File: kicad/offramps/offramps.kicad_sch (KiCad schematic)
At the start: 224 parts, among them J10 Conn_01x04_Socket, J11 Screw_Terminal_01x02, J12 Conn_01x04_Pin, J13 Micro_SD_Card, J14 Conn_01x03_Male, J15 Screw_Terminal_01x02, J16 Conn_01x02_Pin, J17 Conn_01x02_Pin, J3 VITA_57.1_FMC_HPC_Carrier, J4 Conn_01x02_Pin, J5 Conn_Coaxial, J6 Conn_01x03_Male, J7 Conn_Coaxial, J8 Conn_Coaxial, J9 Conn_01x06_Male, Q1 BSS138, Q10 BSS138, Q11 BSS138, Q12 BSS138, Q13 NPN, Q14 NPN, Q15 NPN, Q16 NPN, Q17 BSS138, Q18 BSS138, Q19 NPN, Q2 BSS138, Q25 BSS138, Q26 BSS138, Q27 BSS138, Q28 BSS138, Q29 BSS138, Q3 BSS138, Q30 BSS138, Q4 BSS138, Q5 BSS138, Q6 BSS138, Q7 BSS138, Q8 BSS138, Q9 BSS138, SW1 219-8MST, U1 TXB0108PWR, U10 MCP4725xxx-xCH, U11 LMH6611MK/NOPB, U12 ADC1173CIMTC/NOPB, U13 MCP4725xxx-xCH, U14 POPA2994IDGKR, U15 ADS1114IDGS, U16 LIS2MDLTR, U17 LSM6DSRTR, U18 LTC-4627JR, U19 AMS1117-3.3, U2 TXB0108PWR, U20 LM358DR2G, U3 TXB0108PWR, U4 TXB0108PWR, U5 TXB0108PWR, U6 LMH6611MK/NOPB, U7 ADC1175CIMTC/NOPB, U8 TXB0108PWR, U9 PTMUX4053PWR

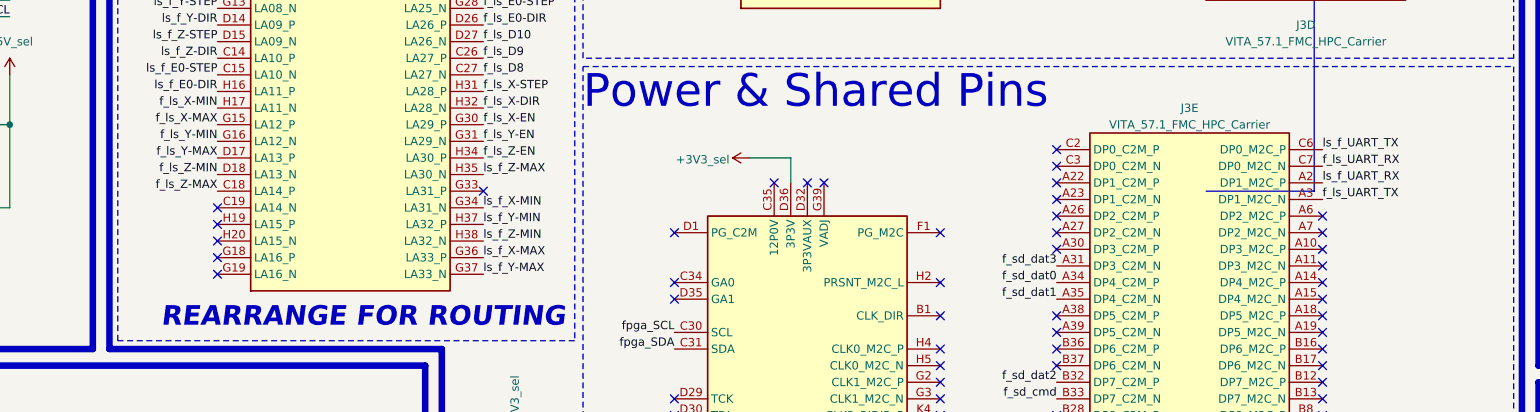
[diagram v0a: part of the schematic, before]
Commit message: Update: Moved UART lines to LPC
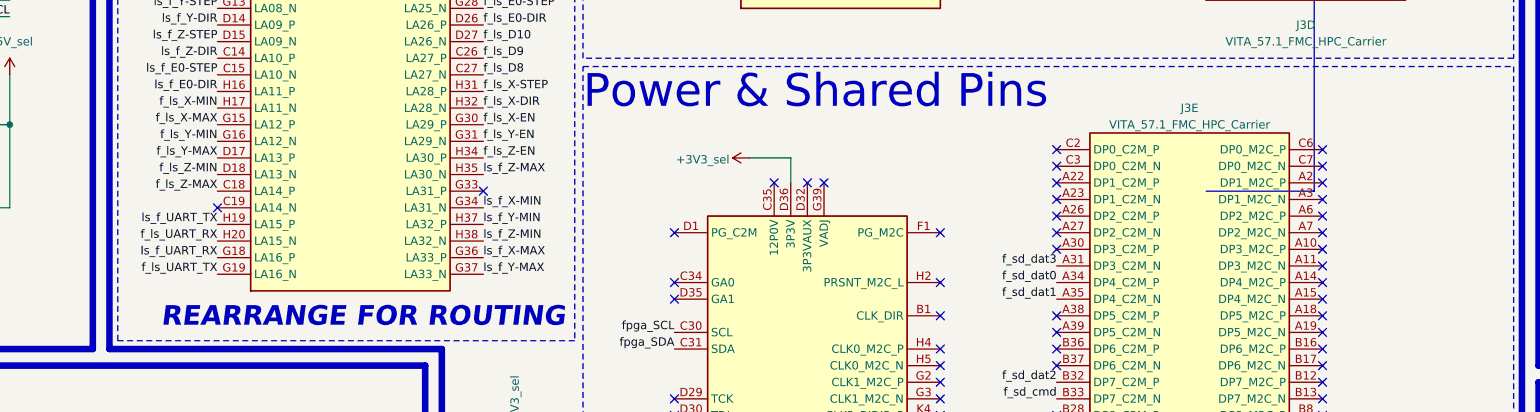
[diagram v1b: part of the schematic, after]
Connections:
- net f_ls_UART_RX: now also J3.H20 (LA15_N); no longer J3.C7 (DP0_M2C_N)
- net f_ls_UART_TX: now also J3.G19 (LA16_N); no longer J3.A3 (DP1_M2C_N)
- net ls_f_UART_RX: now also J3.G18 (LA16_P); no longer J3.A2 (DP1_M2C_P)
- net ls_f_UART_TX: now also J3.H19 (LA15_P); no longer J3.C6 (DP0_M2C_P)
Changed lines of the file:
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@@
 	)
 	(no_connect
+		(at 368.3 132.08)
+	)
+	(no_connect
 		(at 199.39 74.93)
 	)
@@
 	)
 	(no_connect
+		(at 368.3 137.16)
+	)
+	(no_connect
 		(at 368.3 180.34)
 	)
@@
 	)
 	(no_connect
+		(at 368.3 134.62)
+	)
+	(no_connect
+		(at 368.3 139.7)
+	)
+	(no_connect
 		(at 368.3 193.04)
 	)
@@
 	)
 	(no_connect
-		(at 199.39 151.13)
-	)
-	(no_connect
 		(at 368.3 149.86)
 	)
@@
 	)
 	(no_connect
-		(at 199.39 146.05)
-	)
-	(no_connect
 		(at 309.88 144.78)
 	)
 	(no_connect
-		(at 199.39 148.59)
-	)
-	(no_connect
 		(at 269.24 152.4)
 	)
@@
 	)
 	(no_connect
-		(at 199.39 143.51)
-	)
-	(no_connect
 		(at 436.88 148.59)
 	)
@@
 	)
 	(label "ls_f_UART_TX"
-		(at 368.3 132.08 0)
+		(at 199.39 143.51 180)
 		(fields_autoplaced yes)
 		(effects
@@
 				(size 1.27 1.27)
 			)
-			(justify left bottom)
+			(justify right bottom)
 		)
 	)
@@
 	)
 	(label "f_ls_UART_TX"
-		(at 368.3 139.7 0)
+		(at 199.39 151.13 180)
 		(fields_autoplaced yes)
 		(effects
@@
 				(size 1.27 1.27)
 			)
-			(justify left bottom)
+			(justify right bottom)
 		)
 	)
@@
 	)
 	(label "ls_f_UART_RX"
-		(at 368.3 137.16 0)
+		(at 199.39 148.59 180)
 		(fields_autoplaced yes)
 		(effects
@@
 				(size 1.27 1.27)
 			)
-			(justify left bottom)
+			(justify right bottom)
 		)
 	)
@@
 	)
 	(label "f_ls_UART_RX"
-		(at 368.3 134.62 0)
+		(at 199.39 146.05 180)
 		(fields_autoplaced yes)
 		(effects
@@
 				(size 1.27 1.27)
 			)
-			(justify left bottom)
+			(justify right bottom)
 		)
 	)

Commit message: Almost done. Need to flip the FMC connector.
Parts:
- removed J13: Micro_SD_Card, Connector_Card:microSD_HC_Wuerth_693072010801, symbol Connector:Micro_SD_Card
- added J13: Micro_SD_Card_Det1, offramps_lib:SIM-SMD_GT-TF003-H0185-02, symbol Connector:Micro_SD_Card_Det1
- added R80: NP, Resistor_SMD:R_0805_2012Metric, symbol Device:R
- C11, C12, C13, C14, C15, C18, C19, C20, C22, C25, C26, C29, C30, C31: value 100n -> 0.1u; Vendor (none) -> C49678
- C16, C17, C27, C28: Vendor (none) -> C377773
- C32, C34, C36, C38: value 100nF -> 0.1u
- C33: value 10uF -> 10u; Vendor ? -> C440198
- C35: value 220nF -> 220n
- C37: value 100n -> 0.1u
- C39: value 1uF -> 1u
- C43, C44, C45, C46: Vendor (none) -> C440198
- L1, L2: Vendor (none) -> C1046
- Q1, Q10, Q11, Q12, Q17, Q18, Q2, Q25, Q26, Q27, Q28, Q29, Q3, Q30, Q4, Q5, Q6, Q7, Q8, Q9: Vendor (none) -> C2938375
- Q13, Q14, Q15, Q16, Q19: Vendor (none) -> C141788
- R10, R12, R13, R14, R15, R16, R17, R18, R19, R2, R20, R21, R22, R23, R24, R3, R34, R40, R41, R45, R48, R49, R5, R53, R54, R58, R59, R6, R72, R73, R74, R75, R76, R77, R79, R8, R9: Vendor (none) -> C17414
- R11, R26: value 10R -> 10; Vendor (none) -> C17415
- R25, R30: Vendor (none) -> C17594
- R27, R31: Vendor (none) -> C17590
- R32, R33, R52, R57: value 10K -> 10k
- R35, R36, R37, R38, R42, R43, R44, R46, R61: Vendor (none) -> C17408
- R39, R47: Vendor (none) -> C2828783
- R56, R66, R68, R71: Vendor (none) -> C17513
- R64: Vendor (none) -> C17710
- R67, R69, R70, R78: Vendor (none) -> C17477
- SW1: value 219-8MST -> 219-8MSTR; Vendor (none) -> C2842674
- U11, U6: Vendor (none) -> C132099
- U12: value ADC1173CIMTC/NOPB -> ADC1173CIMTCX/NOPB; Vendor (none) -> C701593
- U14: value POPA2994IDGKR -> OPA2994IDGKR; Vendor (none) -> C22399234
- U15: value ADS1114IDGS -> ADS1114IDGSR; Vendor (none) -> C174291
- U7: value ADC1175CIMTC/NOPB -> ADC1175-50CIMTCX/NOPB; Vendor (none) -> C91171
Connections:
- net +3V3_filt: now also C25.1, U11.5 (~DIS), U11.6 (V+); no longer C22.1
- net +3V3_sel: now also C22.1, J13.4 (VDD), R80.1
- net +5V_filt: no longer C25.1, U11.5 (~DIS), U11.6 (V+)
- net GND: now also J13.10 (SHIELD), J13.6 (VSS)
- net f_sd_clk: now also J13.5 (CLK)
- net f_sd_cmd: now also J13.3 (CMD)
- net f_sd_dat0: now also J13.7 (DAT0)
- net f_sd_dat1: now also J13.8 (DAT1)
- net f_sd_dat2: now also J13.1 (DAT2)
- net f_sd_dat3: now also J13.2 (DAT3/CD)
- net f_sd_det: now reaches J3.A38 (DP5_C2M_P)
- net f_sd_det: now also J13.9 (DET), R80.2
- no-connect marks 139 -> 138

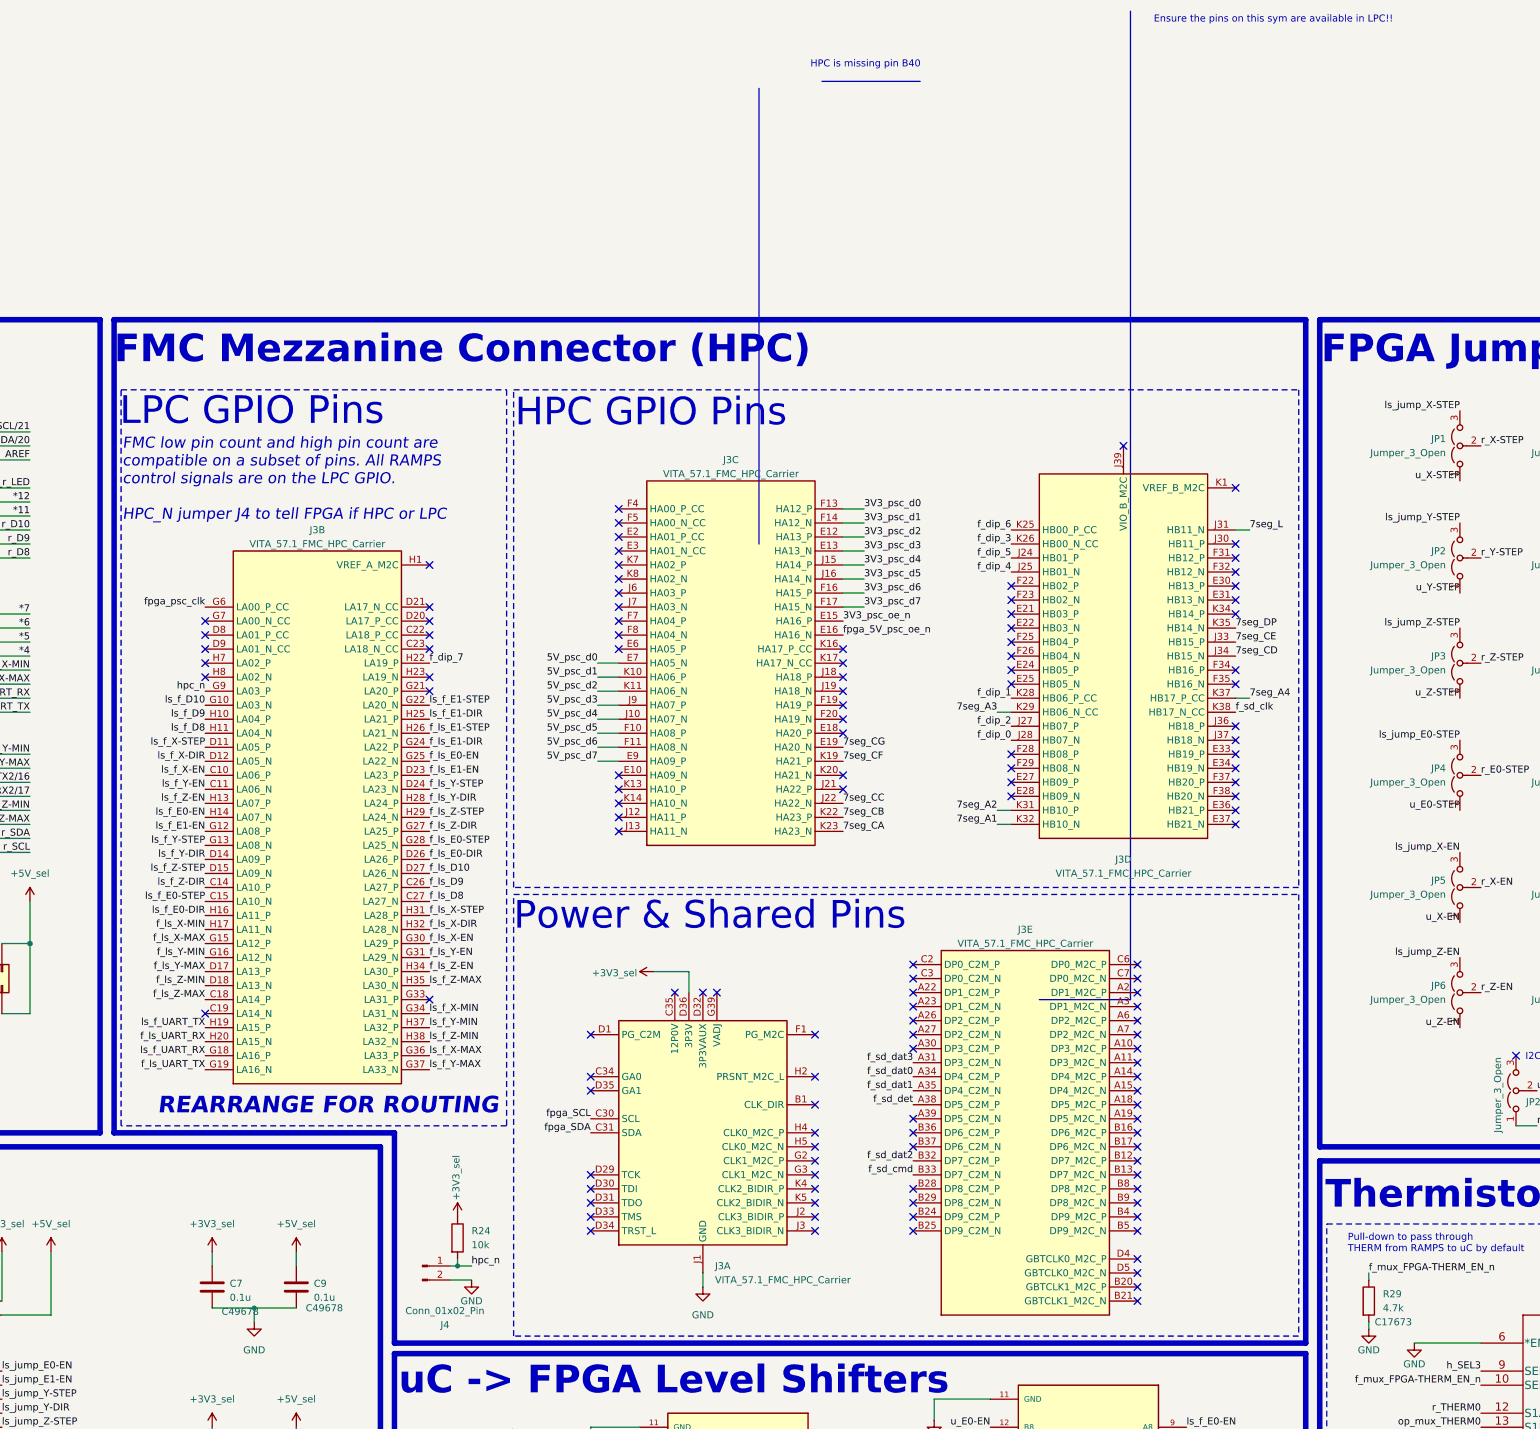
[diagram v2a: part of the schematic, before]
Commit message: UPDATE: Rotated FMC by 180 degrees and rerouted all signals
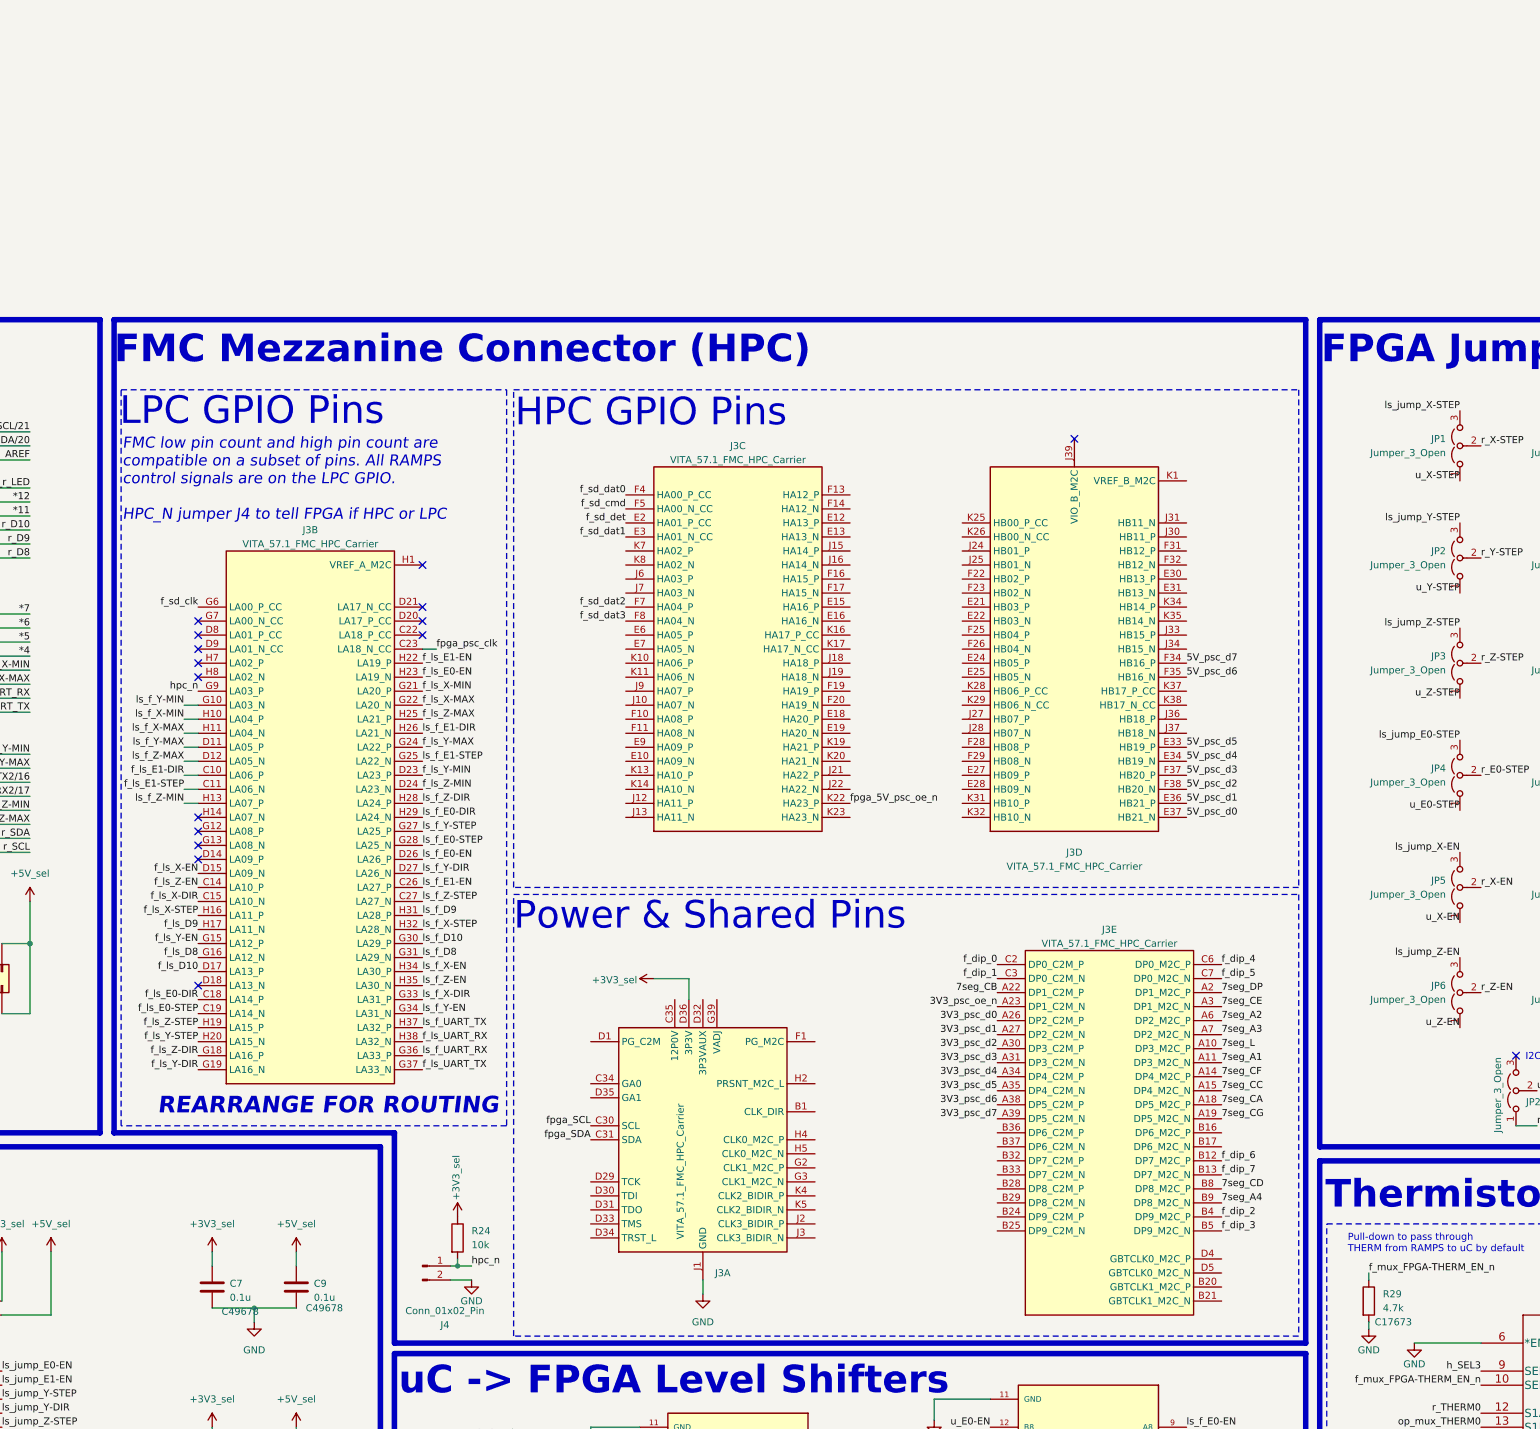
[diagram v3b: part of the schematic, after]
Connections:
- net 3V3_psc_d0: now also J3.A26 (DP2_C2M_P); no longer J3.F13 (HA12_P)
- net 3V3_psc_d1: now also J3.A27 (DP2_C2M_N); no longer J3.F14 (HA12_N)
- net 3V3_psc_d2: now also J3.A30 (DP3_C2M_P); no longer J3.E12 (HA13_P)
- net 3V3_psc_d3: now also J3.A31 (DP3_C2M_N); no longer J3.E13 (HA13_N)
- net 3V3_psc_d4: now also J3.A34 (DP4_C2M_P); no longer J3.J15 (HA14_P)
- net 3V3_psc_d5: now also J3.A35 (DP4_C2M_N); no longer J3.J16 (HA14_N)
- net 3V3_psc_d6: now also J3.A38 (DP5_C2M_P); no longer J3.F16 (HA15_P)
- net 3V3_psc_d7: now also J3.A39 (DP5_C2M_N); no longer J3.F17 (HA15_N)
- net 3V3_psc_oe_n: now also J3.A23 (DP1_C2M_N); no longer J3.E15 (HA16_P)
- net 5V_psc_d0: now also J3.E37 (HB21_N); no longer J3.E7 (HA05_N)
- net 5V_psc_d1: now also J3.E36 (HB21_P); no longer J3.K10 (HA06_P)
- net 5V_psc_d2: now also J3.F38 (HB20_N); no longer J3.K11 (HA06_N)
- net 5V_psc_d3: now also J3.F37 (HB20_P); no longer J3.J9 (HA07_P)
- net 5V_psc_d4: now also J3.E34 (HB19_N); no longer J3.J10 (HA07_N)
- net 5V_psc_d5: now also J3.E33 (HB19_P); no longer J3.F10 (HA08_P)
- net 5V_psc_d6: now also J3.F35 (HB16_N); no longer J3.F11 (HA08_N)
- net 5V_psc_d7: now also J3.F34 (HB16_P); no longer J3.E9 (HA09_P)
- net 7seg_A1: now also J3.A11 (DP3_M2C_N); no longer J3.K32 (HB10_N)
- net 7seg_A2: now also J3.A6 (DP2_M2C_P); no longer J3.K31 (HB10_P)
- net 7seg_A3: now also J3.A7 (DP2_M2C_N); no longer J3.K29 (HB06_N_CC)
- net 7seg_A4: now also J3.B9 (DP8_M2C_N); no longer J3.K37 (HB17_P_CC)
- net 7seg_CA: now also J3.A18 (DP5_M2C_P); no longer J3.K23 (HA23_N)
- net 7seg_CB: now also J3.A22 (DP1_C2M_P); no longer J3.K22 (HA23_P)
- net 7seg_CC: now also J3.A15 (DP4_M2C_N); no longer J3.J22 (HA22_N)
- net 7seg_CD: now also J3.B8 (DP8_M2C_P); no longer J3.J34 (HB15_N)
- net 7seg_CE: now also J3.A3 (DP1_M2C_N); no longer J3.J33 (HB15_P)
- net 7seg_CF: now also J3.A14 (DP4_M2C_P); no longer J3.K19 (HA21_P)
- net 7seg_CG: now also J3.A19 (DP5_M2C_N); no longer J3.E19 (HA20_N)
- net 7seg_DP: now also J3.A2 (DP1_M2C_P); no longer J3.K35 (HB14_N)
- net 7seg_L: now also J3.A10 (DP3_M2C_P); no longer J3.J31 (HB11_N)
- net f_dip_0: now also J3.C2 (DP0_C2M_P); no longer J3.J28 (HB07_N)
- net f_dip_1: now also J3.C3 (DP0_C2M_N); no longer J3.K28 (HB06_P_CC)
- net f_dip_2: now also J3.B4 (DP9_M2C_P); no longer J3.J27 (HB07_P)
- net f_dip_3: now also J3.B5 (DP9_M2C_N); no longer J3.K26 (HB00_N_CC)
- net f_dip_4: now also J3.C6 (DP0_M2C_P); no longer J3.J25 (HB01_N)
- net f_dip_5: now also J3.C7 (DP0_M2C_N); no longer J3.J24 (HB01_P)
- net f_dip_6: now also J3.B12 (DP7_M2C_P); no longer J3.K25 (HB00_P_CC)
- net f_dip_7: now also J3.B13 (DP7_M2C_N); no longer J3.H22 (LA19_P)
- net f_ls_D10: now also J3.D17 (LA13_P); no longer J3.D27 (LA26_N)
- net f_ls_D8: now also J3.G16 (LA12_N); no longer J3.C27 (LA27_N)
- net f_ls_D9: now also J3.H17 (LA11_N); no longer J3.C26 (LA27_P)
- net f_ls_E0-DIR: now also J3.C18 (LA14_P); no longer J3.D26 (LA26_P)
- net f_ls_E0-EN: now also J3.H23 (LA19_N); no longer J3.G25 (LA22_N)
- net f_ls_E0-STEP: now also J3.C19 (LA14_N); no longer J3.G28 (LA25_N)
- net f_ls_E1-DIR: now also J3.C10 (LA06_P); no longer J3.G24 (LA22_P)
- net f_ls_E1-EN: now also J3.H22 (LA19_P); no longer J3.D23 (LA23_P)
- net f_ls_E1-STEP: now also J3.C11 (LA06_N); no longer J3.H26 (LA21_N)
- net f_ls_UART_RX: now also J3.H38 (LA32_N); no longer J3.H20 (LA15_N)
- net f_ls_UART_TX: now also J3.G37 (LA33_N); no longer J3.G19 (LA16_N)
- net f_ls_X-DIR: now also J3.C15 (LA10_N); no longer J3.H32 (LA28_N)
- net f_ls_X-EN: now also J3.D15 (LA09_N); no longer J3.G30 (LA29_P)
- net f_ls_X-MAX: now also J3.G22 (LA20_N); no longer J3.G15 (LA12_P)
- net f_ls_X-MIN: now also J3.G21 (LA20_P); no longer J3.H17 (LA11_N)
- net f_ls_X-STEP: now also J3.H16 (LA11_P); no longer J3.H31 (LA28_P)
- net f_ls_Y-DIR: now also J3.G19 (LA16_N); no longer J3.H28 (LA24_P)
- net f_ls_Y-EN: now also J3.G15 (LA12_P); no longer J3.G31 (LA29_N)
- net f_ls_Y-MAX: now also J3.G24 (LA22_P); no longer J3.D17 (LA13_P)
- net f_ls_Y-MIN: now also J3.D23 (LA23_P); no longer J3.G16 (LA12_N)
- net f_ls_Y-STEP: now also J3.H20 (LA15_N); no longer J3.D24 (LA23_N)
- net f_ls_Z-DIR: now also J3.G18 (LA16_P); no longer J3.G27 (LA25_P)
- net f_ls_Z-EN: now also J3.C14 (LA10_P); no longer J3.H34 (LA30_P)
- net f_ls_Z-MAX: now also J3.H25 (LA21_P); no longer J3.C18 (LA14_P)
- net f_ls_Z-MIN: now also J3.D24 (LA23_N); no longer J3.D18 (LA13_N)
- net f_ls_Z-STEP: now also J3.H19 (LA15_P); no longer J3.H29 (LA24_N)
- net f_sd_clk: now also J3.G6 (LA00_P_CC); no longer J3.K38 (HB17_N_CC)
- net f_sd_cmd: now also J3.F5 (HA00_N_CC); no longer J3.B33 (DP7_C2M_N)
- net f_sd_dat0: now also J3.F4 (HA00_P_CC); no longer J3.A34 (DP4_C2M_P)
- net f_sd_dat1: now also J3.E3 (HA01_N_CC); no longer J3.A35 (DP4_C2M_N)
- net f_sd_dat2: now also J3.F7 (HA04_P); no longer J3.B32 (DP7_C2M_P)
- net f_sd_dat3: now also J3.F8 (HA04_N); no longer J3.A31 (DP3_C2M_N)
- net f_sd_det: now also J3.E2 (HA01_P_CC); no longer J3.A38 (DP5_C2M_P)
- net fpga_5V_psc_oe_n: now also J3.K22 (HA23_P); no longer J3.E16 (HA16_N)
- net fpga_psc_clk: now also J3.C23 (LA18_N_CC); no longer J3.G6 (LA00_P_CC)
- net ls_f_D10: now also J3.G30 (LA29_P); no longer J3.G10 (LA03_N)
- net ls_f_D8: now also J3.G31 (LA29_N); no longer J3.H11 (LA04_N)
- net ls_f_D9: now also J3.H31 (LA28_P); no longer J3.H10 (LA04_P)
- net ls_f_E0-DIR: now also J3.H29 (LA24_N); no longer J3.H16 (LA11_P)
- net ls_f_E0-EN: now also J3.D26 (LA26_P); no longer J3.H14 (LA07_N)
- net ls_f_E0-STEP: now also J3.G28 (LA25_N); no longer J3.C15 (LA10_N)
- net ls_f_E1-DIR: now also J3.H26 (LA21_N); no longer J3.H25 (LA21_P)
- net ls_f_E1-EN: now also J3.C26 (LA27_P); no longer J3.G12 (LA08_P)
- net ls_f_E1-STEP: now also J3.G25 (LA22_N); no longer J3.G22 (LA20_N)
- net ls_f_UART_RX: now also J3.G36 (LA33_P); no longer J3.G18 (LA16_P)
- net ls_f_UART_TX: now also J3.H37 (LA32_P); no longer J3.H19 (LA15_P)
- net ls_f_X-DIR: now also J3.G33 (LA31_P); no longer J3.D12 (LA05_N)
- net ls_f_X-EN: now also J3.H34 (LA30_P); no longer J3.C10 (LA06_P)
- net ls_f_X-MAX: now also J3.H11 (LA04_N); no longer J3.G36 (LA33_P)
- net ls_f_X-MIN: now also J3.H10 (LA04_P); no longer J3.G34 (LA31_N)
- net ls_f_X-STEP: now also J3.H32 (LA28_N); no longer J3.D11 (LA05_P)
- net ls_f_Y-DIR: now also J3.D27 (LA26_N); no longer J3.D14 (LA09_P)
- net ls_f_Y-EN: now also J3.G34 (LA31_N); no longer J3.C11 (LA06_N)
- net ls_f_Y-MAX: now also J3.D11 (LA05_P); no longer J3.G37 (LA33_N)
- net ls_f_Y-MIN: now also J3.G10 (LA03_N); no longer J3.H37 (LA32_P)
- net ls_f_Y-STEP: now also J3.G27 (LA25_P); no longer J3.G13 (LA08_N)
- net ls_f_Z-DIR: now also J3.H28 (LA24_P); no longer J3.C14 (LA10_P)
- net ls_f_Z-EN: now also J3.H35 (LA30_N); no longer J3.H13 (LA07_P)
- net ls_f_Z-MAX: now also J3.D12 (LA05_N); no longer J3.H35 (LA30_N)
- net ls_f_Z-MIN: now also J3.H13 (LA07_P); no longer J3.H38 (LA32_N)
- net ls_f_Z-STEP: now also J3.C27 (LA27_N); no longer J3.D15 (LA09_N)
- no-connect marks 138 -> 24
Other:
- note removed: "Ensure the pins on this sym are available in LPC!!"
- note removed: "HPC is missing pin B40"
- moved on the sheet: J3A, J3B, J3C, J3D, J3E
